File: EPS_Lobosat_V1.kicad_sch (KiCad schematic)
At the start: 57 parts, among them Q1 FS8205A, Q2 FS8205A, U1 LMZM33602RLRR, U10 STPS140ZY, U2 LT3652EMSE_PBF, U3 DW01A, U4 ADS1015IRUGR, U5 STPS140ZY, U6 ADS1015IRUGR, U7 STPS140ZY, U8 LT3652EMSE_PBF, U9 DW01A

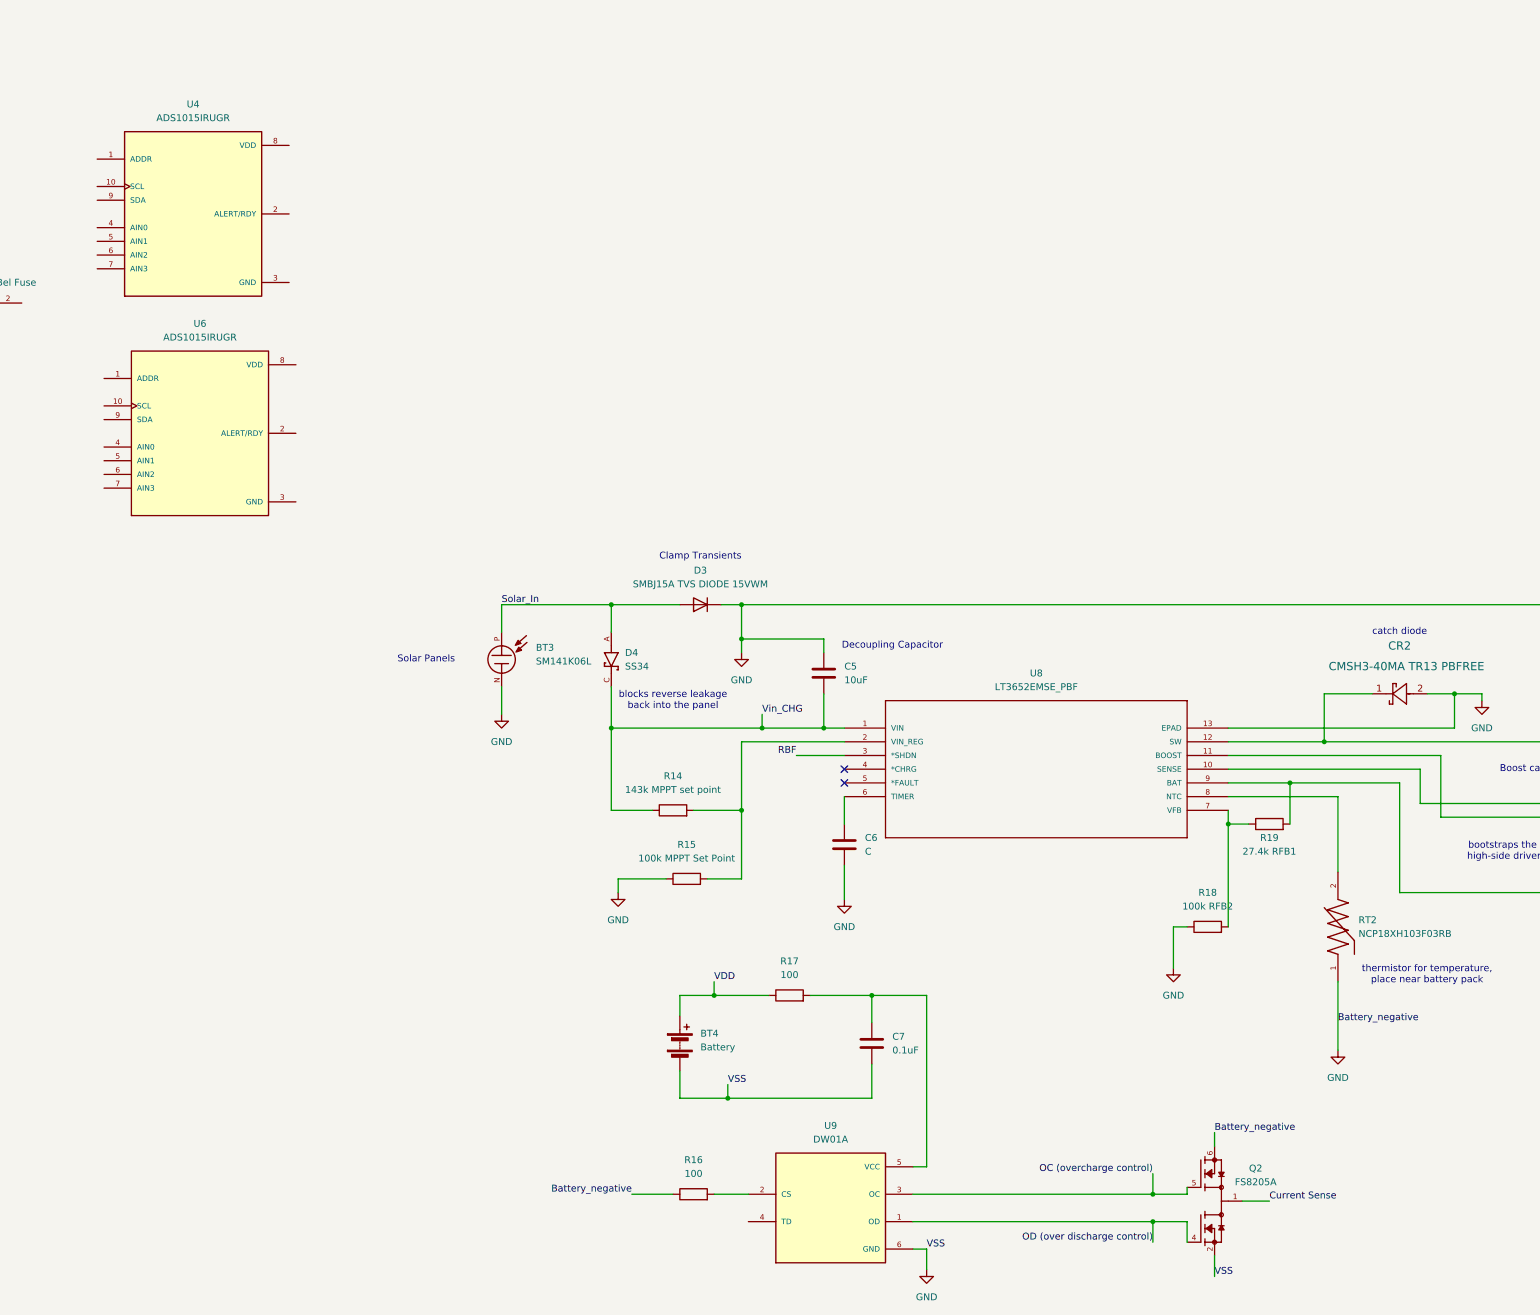
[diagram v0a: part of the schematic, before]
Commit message: new Battery ICs: BQ29209 and the S-8252
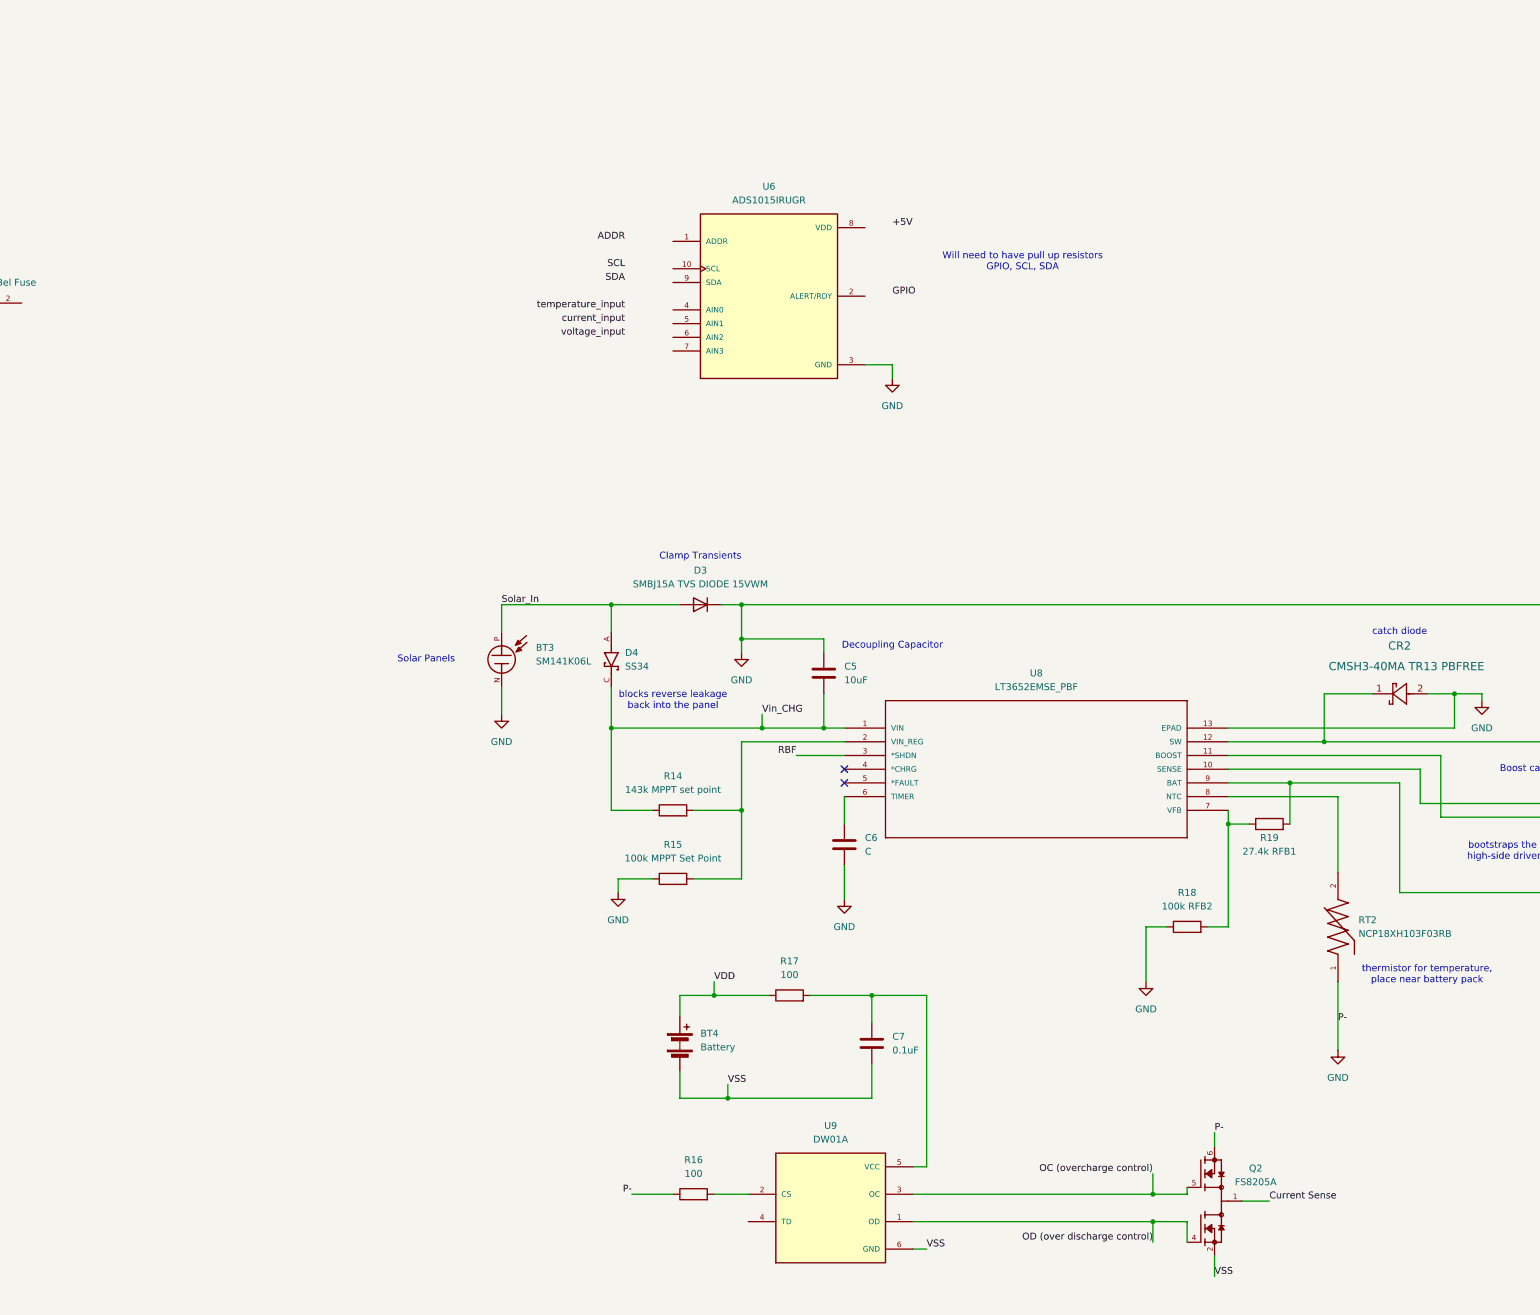
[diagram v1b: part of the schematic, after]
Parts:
- removed U4: ADS1015IRUGR, ADS1015IRUGR:IC_ADS1015IRUGR, symbol ADS1015IRUGR:ADS1015IRUGR
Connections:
- net GND: now also U6.3 (GND); no longer Q1.6, Q1.7, RT1.2, U2.8 (NTC)
- new net Battery_negative: Q1.6, Q1.7, RT1.2, U2.8 (NTC)
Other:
- note added: "Will need to have pull up resistors GPIO, SCL, SDA"
- moved on the sheet: R15, R18, U6
